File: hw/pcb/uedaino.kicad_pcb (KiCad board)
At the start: 2 copper layers, 34 parts, among them IC1 ATMEGA328P-A, P1 CN_PWR, P2 CN_UART, P3 CN_HEADER1, P4 CN_I2C, P5 CN_HEADER2, P6 CN_ICSP, SW1 SW_PUSH, U1 AP1117, Y1 16MHz

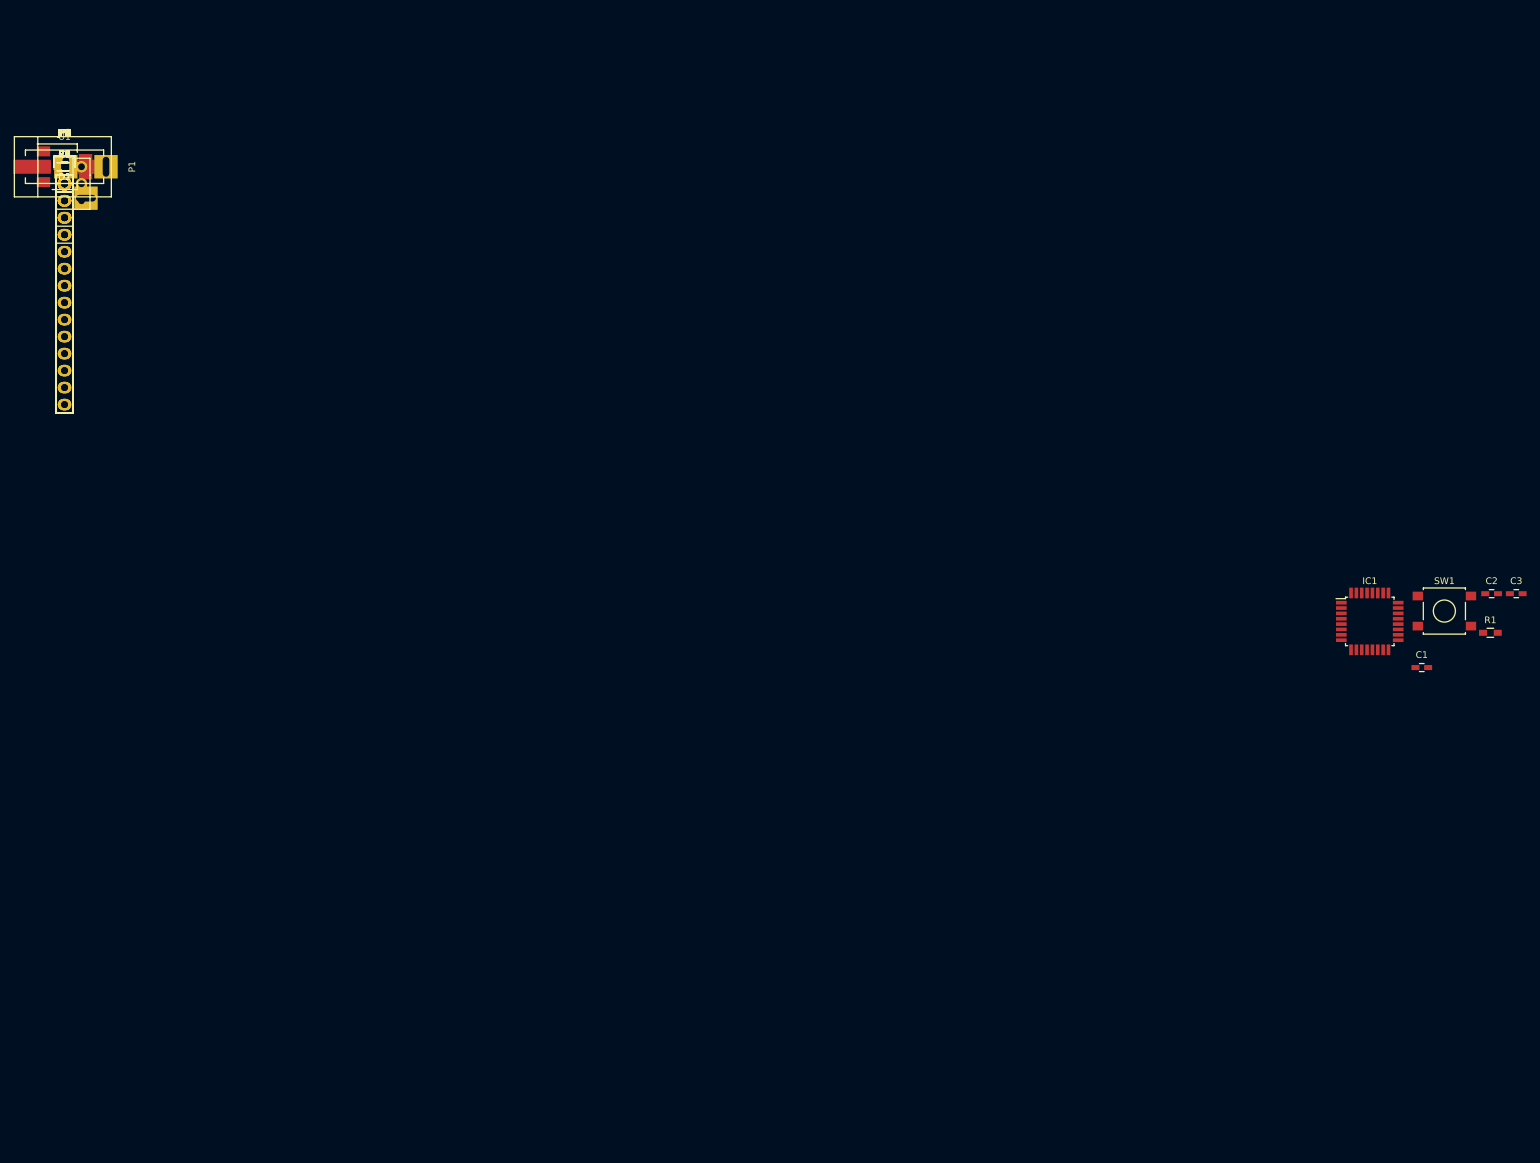
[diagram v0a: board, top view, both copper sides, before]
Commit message: Roughly placed the components
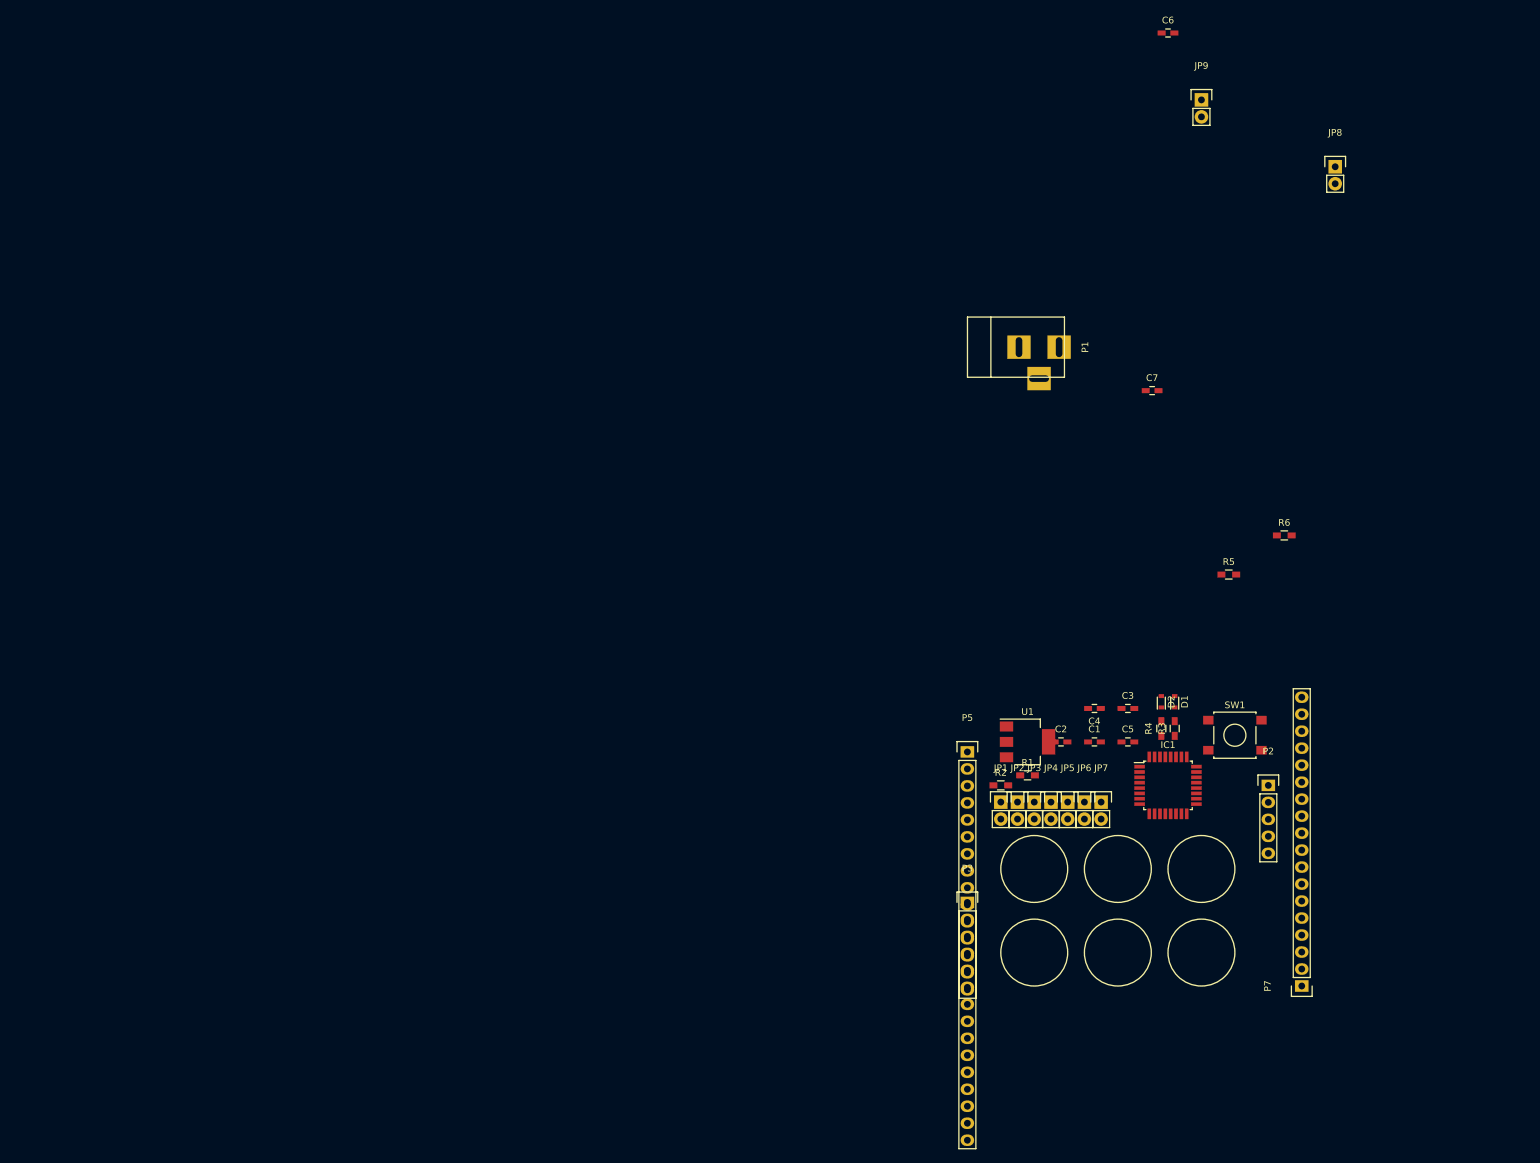
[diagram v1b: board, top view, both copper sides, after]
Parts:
- removed P4: CN_I2C, Pin_Headers:Pin_Header_Straight_1x04
- removed P6: CN_ICSP, Pin_Headers:Pin_Header_Straight_2x03
- removed Y1: 16MHz, Crystals:Crystal_HC49-SD_SMD
- added P7: DIGITAL, Socket_Strips:Socket_Strip_Straight_1x18, F.Cu at (185.0, 122.5)
- P3: value CN_HEADER1 -> ANALOG_IN
- P5: value CN_HEADER2 -> POWER
- moved P2 202.4 mm to (180.0, 92.5)
- moved R6 190.5 mm to (182.4, 55.1)
- moved JP8 190.0 mm to (190.0, 0.00)
- moved R3 186.0 mm to (166.0, 84.0), turned to 90 degrees
- moved R5 184.5 mm to (174.1, 61.0)
- moved D1 184.3 mm to (166.0, 80.0), turned to 90 degrees
- moved R4 184.3 mm to (164.0, 84.0), turned to 90 degrees
- moved D2 182.5 mm to (164.0, 80.0), turned to 90 degrees
- moved JP7 181.8 mm to (155.0, 95.0)
- moved C5 180.8 mm to (159.0, 86.0)
- moved JP6 179.7 mm to (152.5, 95.0)
- moved JP5 177.6 mm to (150.0, 95.0)
- moved JP4 175.4 mm to (147.5, 95.0)
- moved P3 174.1 mm to (135.0, 110.0)
- moved C4 174.0 mm to (154.0, 81.0), turned to 180 degrees
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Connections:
- net Net-(C2-Pad1) renamed /AREF
- IC1 pad 19: /A6 -> Net-(IC1-Pad19)
- IC1 pad 22: /A7 -> Net-(IC1-Pad22)
- IC1 pad 7: /XT1 -> Net-(IC1-Pad7)
- IC1 pad 8: /XT2 -> Net-(IC1-Pad8)
- P1 pad 1: (no net) -> Net-(P1-Pad1)
- P2 pad 3: (no net) -> /PWR_USB
- P3 pad 1: /TXD -> /A0
- P3 pad 10: /D7 -> (no net)
- P3 pad 11: /D8 -> (no net)
- P3 pad 12: /D9 -> (no net)
- P3 pad 13: /D10 -> (no net)
- P3 pad 14: /D11 -> (no net)
- P3 pad 15: /D12 -> (no net)
- P3 pad 2: /RXD -> /A1
- P3 pad 3: /RESET -> /A2
- P3 pad 4: GND -> /A3
- P3 pad 5: /D2 -> /A4/SDA
- P3 pad 6: /D3 -> /A5/SCL
- P3 pad 7: /D4 -> (no net)
- P3 pad 8: /D5 -> (no net)
- P3 pad 9: /D6 -> (no net)
- P5 pad 1: (no net) -> Net-(P5-Pad1)
- P5 pad 10: /A2 -> (no net)
- P5 pad 11: /A1 -> (no net)
- P5 pad 12: /A0 -> (no net)
- P5 pad 14: +3V3 -> (no net)
- P5 pad 15: /D13 -> (no net)
- P5 pad 2: GND -> +5V
- P5 pad 4: +5V -> +3V3
- P5 pad 5: /A7 -> +5V
- P5 pad 6: /A6 -> GND
- P5 pad 7: /A5/SCL -> GND
- P5 pad 8: /A4/SDA -> +5V
- P5 pad 9: /A3 -> (no net)
- U1 pad 4: (no net) -> +3V3
